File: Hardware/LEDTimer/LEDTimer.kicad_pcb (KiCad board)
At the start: 4 copper layers, 38 x 27.3 mm, 36 parts, among them J2 LED, J3 PWR, SW1 SW_Push, SW2 SW_Push, SW3 SW_Push, SW4 SW_BAT, U1 AP7383-36WW7, U2 PIC16F1825, U3 Display_128x64_096_I2C, U4 BCR_421U_E6327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

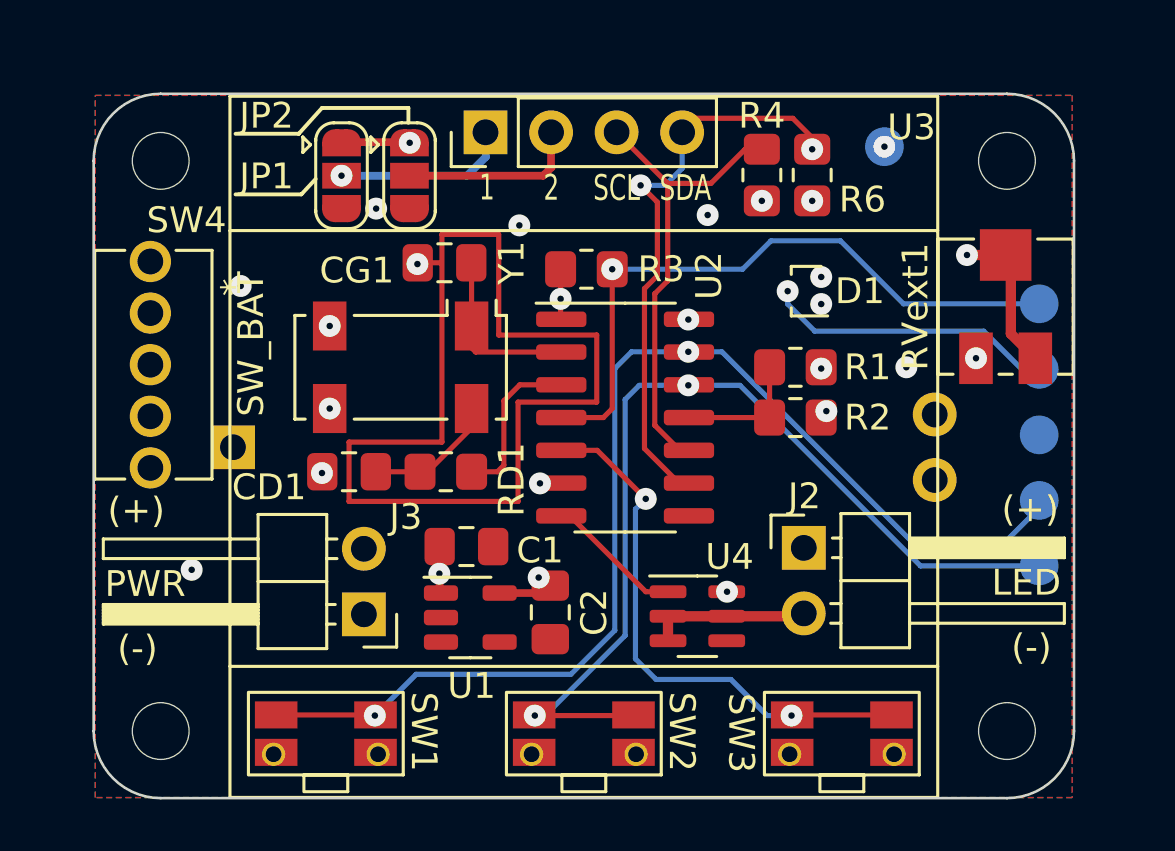
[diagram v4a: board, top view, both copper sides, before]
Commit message: PCB: re-purpose the switch as main power switch, add a transistor to LDO_SENSE for protection
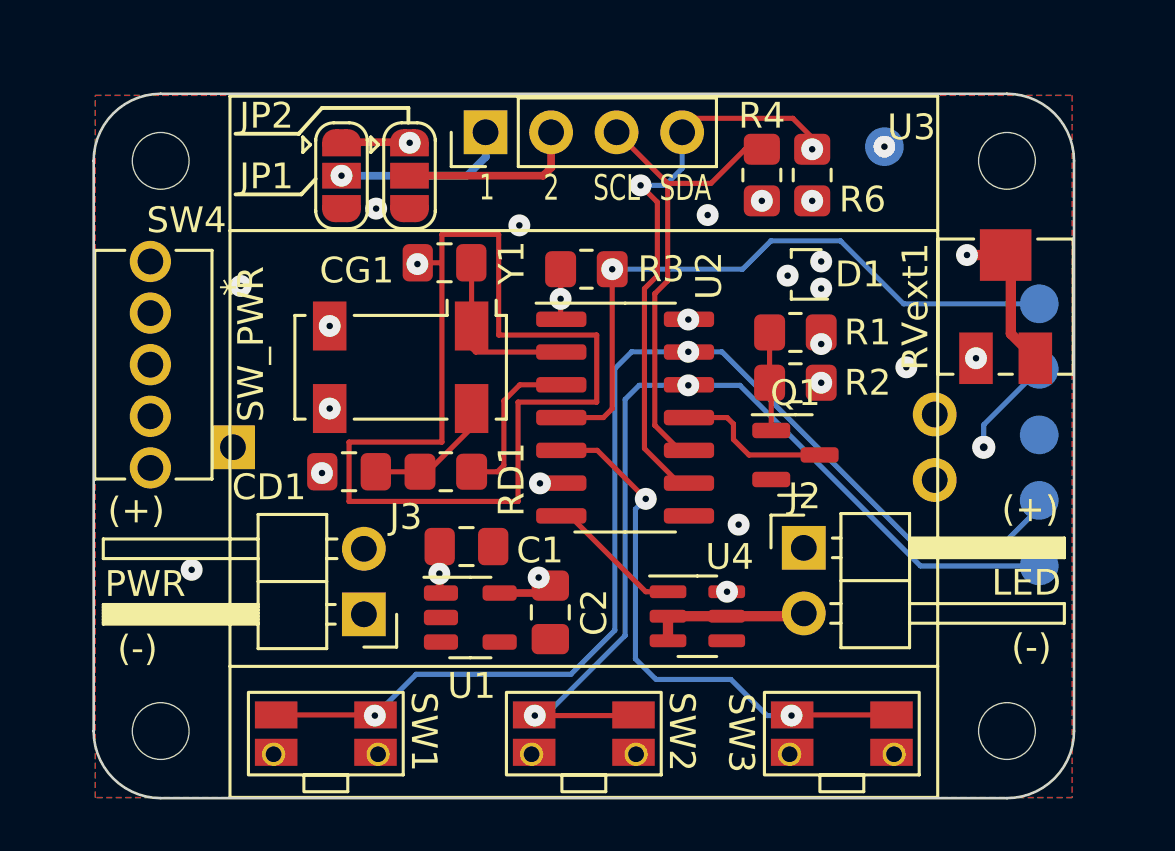
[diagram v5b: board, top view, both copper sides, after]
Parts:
- added Q1: S8050, Package_TO_SOT_SMD:SOT-23, F.Cu at (148.5, 93.5)
- SW4: value SW_BAT -> SW_PWR
- moved R1 1.35 mm to (148.5, 88.8)
- moved R2 1.35 mm to (148.5, 90.7)
- moved D1 0.65 mm to (148.8, 86.5)
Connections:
- BT1 pad 2: Net-(BT1-Pad2) -> Net-(D1-Pad2)
- D1 pad 3: +3V3 -> Net-(D1-Pad3)
- R1 pad 2: /LDO_SENSE -> Net-(R1-Pad2)
- R2 pad 1: /LDO_SENSE -> Net-(R1-Pad2)
- SW4 pad 2: Net-(D1-Pad2) -> +3V3
- SW4 pad 3: Net-(BT1-Pad2) -> Net-(D1-Pad3)
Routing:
- net Net-(BT1-Pad2): track 47.9 -> 0.00 mm
- net Net-(D1-Pad3): track 0.00 -> 41.1 mm, vias 0 -> 1
- net Net-(D1-Pad2): track 48.6 -> 11.6 mm
- net +3V3: track 40.7 -> 59.0 mm
- net Net-(R1-Pad2): track 0.00 -> 3.83 mm
- net Net-(C2-Pad1): track 19.7 -> 20.6 mm
- net /LDO_SENSE: track 5.08 -> 6.01 mm
- net GND: vias 13 -> 14
